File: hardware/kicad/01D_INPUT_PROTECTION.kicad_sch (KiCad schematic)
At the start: 1 part, among them U401 TPS26631PWPT CANDIDATE - NOT 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

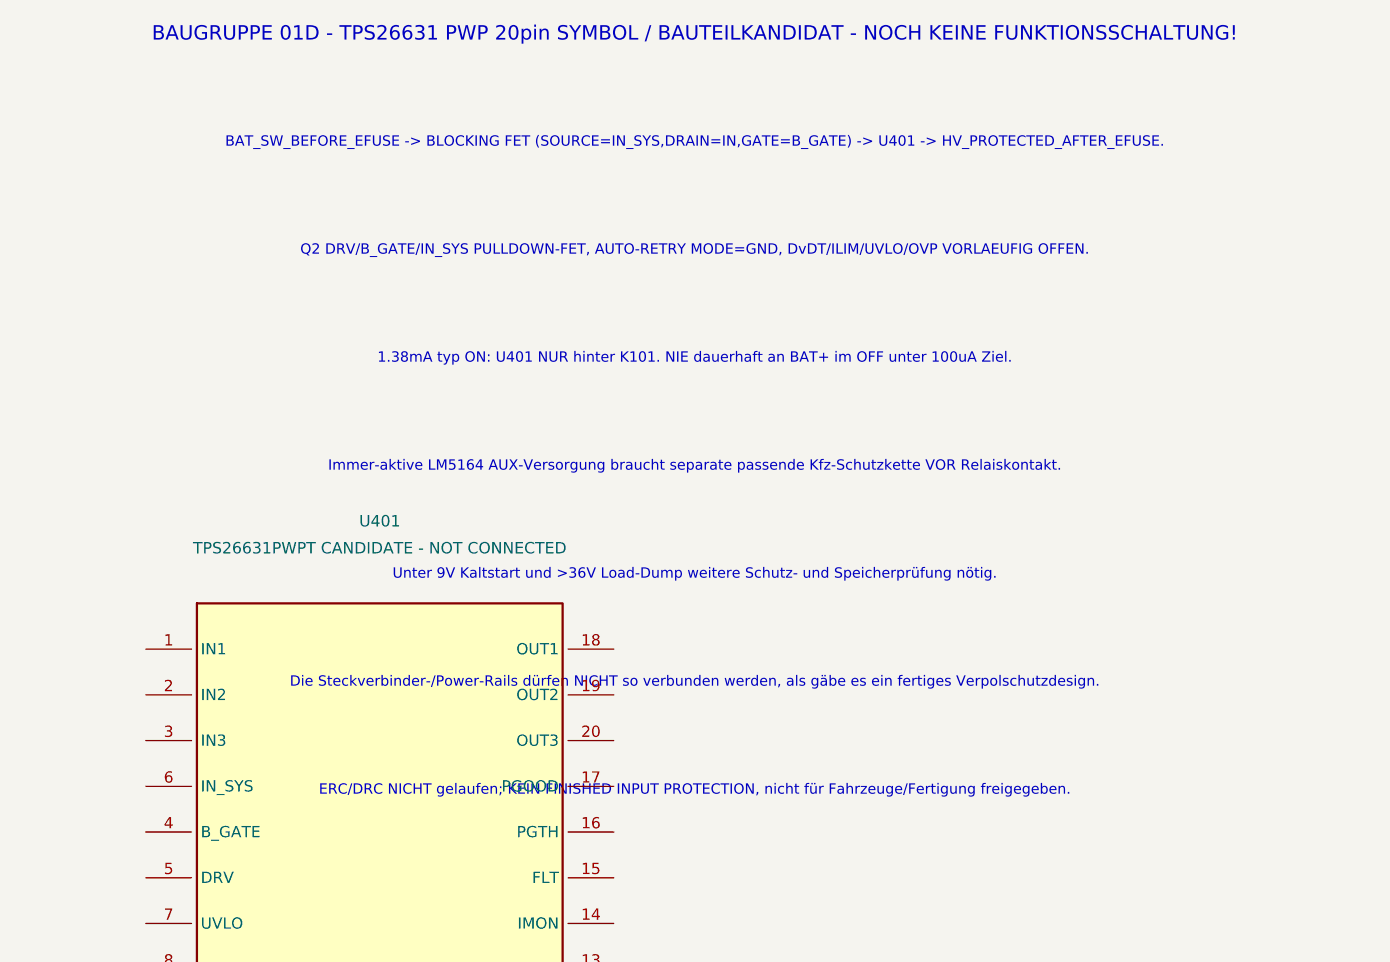
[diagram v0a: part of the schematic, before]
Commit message: kicad(power): flag relay versus eFuse overcurrent blocker in 01D
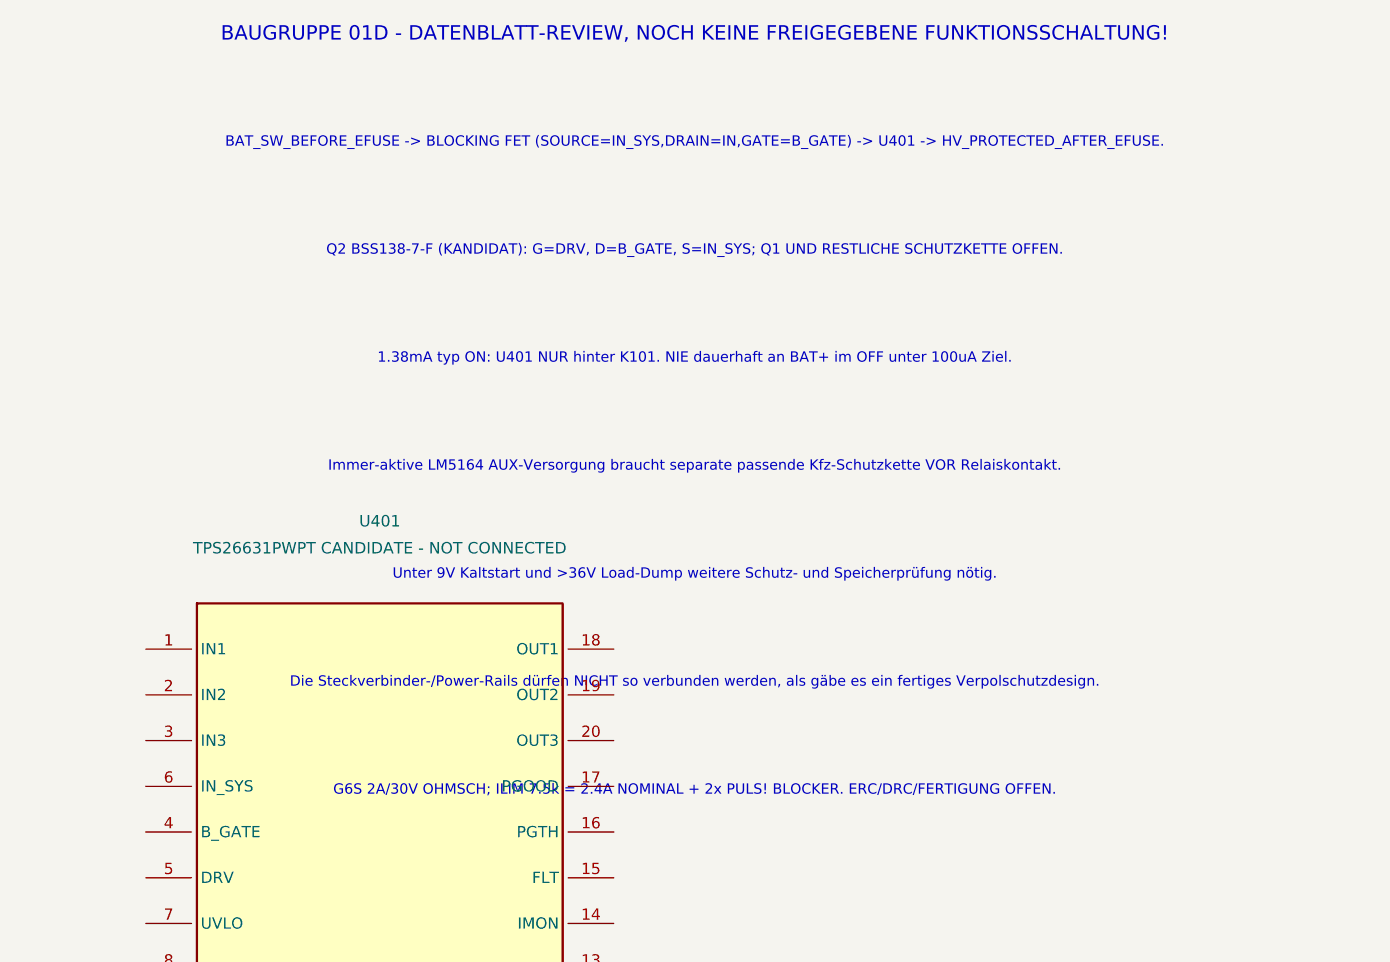
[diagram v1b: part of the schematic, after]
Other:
- note added: "BAUGRUPPE 01D - DATENBLATT-REVIEW, NOCH KEINE FREIGEGEBENE FUNKTIONSSCHALTUNG!"
- note added: "G6S 2A/30V OHMSCH; ILIM 7.5k = 2.4A NOMINAL + 2x PULS! BLOCKER. ERC/DRC/FERTIGUNG OFFEN."
- note added: "Q2 BSS138-7-F (KANDIDAT): G=DRV, D=B_GATE, S=IN_SYS; Q1 UND RESTLICHE SCHUTZKETTE OFFEN."
- note removed: "BAUGRUPPE 01D - TPS26631 PWP 20pin SYMBOL / BAUTEILKANDIDAT - NOCH KEINE FUNKTIONSSCHALTUNG!"
- note removed: "ERC/DRC NICHT gelaufen; KEIN FINISHED INPUT PROTECTION, nicht für Fahrzeuge/Fertigung freigegeben."
- note removed: "Q2 DRV/B_GATE/IN_SYS PULLDOWN-FET, AUTO-RETRY MODE=GND, DvDT/ILIM/UVLO/OVP VORLAEUFIG OFFEN."
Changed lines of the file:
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@@
 (kicad_sch (version 20250114) (generator "eeschema")
 (paper "A3")
-(title_block (title "TripTracer V1 - Eingangsschutz/eFuse Kandidat") (date "2026-10-13") (rev "a4 / SYMBOL ONLY / NOT CONNECTED / NOT ERC-TESTED"))
+(title_block (title "TripTracer V1 - Eingangsschutz/eFuse Kandidat") (date "2026-10-13") (rev "a5 / DESIGN GATE OPEN / NO WIRING / NO ERC"))
 (symbol (lib_id "TripTracer_V1:TPS26631_PWP") (at 171 112 0) (unit 1) (exclude_from_sim no) (in_bom yes) (on_board yes) (dnp no)
 (property "Reference" "U401" (at 171 80 0) (effects (font (size 1.27 1.27))))
@@
 (pin "12")
 (instances (project "TripTracer_V1" (path "/a26d9b0c-7f10-4e5a-a65f-000000000064/a26d9b0c-7f10-4e5a-a65f-000000000065/72346f29-23d6-4849-8604-2156cfdc44a1" (reference "U401") (unit 1)))))
-(text "BAUGRUPPE 01D - TPS26631 PWP 20pin SYMBOL / BAUTEILKANDIDAT - NOCH KEINE FUNKTIONSSCHALTUNG!" (at 206 26 0) (effects (font (size 1.6 1.6))))
+(text "BAUGRUPPE 01D - DATENBLATT-REVIEW, NOCH KEINE FREIGEGEBENE FUNKTIONSSCHALTUNG!" (at 206 26 0) (effects (font (size 1.6 1.6))))
 (text "BAT_SW_BEFORE_EFUSE -> BLOCKING FET (SOURCE=IN_SYS,DRAIN=IN,GATE=B_GATE) -> U401 -> HV_PROTECTED_AFTER_EFUSE." (at 206 38 0) (effects (font (size 1.15 1.15))))
-(text "Q2 DRV/B_GATE/IN_SYS PULLDOWN-FET, AUTO-RETRY MODE=GND, DvDT/ILIM/UVLO/OVP VORLAEUFIG OFFEN." (at 206 50 0) (effects (font (size 1.15 1.15))))
+(text "Q2 BSS138-7-F (KANDIDAT): G=DRV, D=B_GATE, S=IN_SYS; Q1 UND RESTLICHE SCHUTZKETTE OFFEN." (at 206 50 0) (effects (font (size 1.15 1.15))))
 (text "1.38mA typ ON: U401 NUR hinter K101. NIE dauerhaft an BAT+ im OFF unter 100uA Ziel." (at 206 62 0) (effects (font (size 1.15 1.15))))
 (text "Immer-aktive LM5164 AUX-Versorgung braucht separate passende Kfz-Schutzkette VOR Relaiskontakt." (at 206 74 0) (effects (font (size 1.15 1.15))))
 (text "Unter 9V Kaltstart und >36V Load-Dump weitere Schutz- und Speicherprüfung nötig." (at 206 86 0) (effects (font (size 1.15 1.15))))
 (text "Die Steckverbinder-/Power-Rails dürfen NICHT so verbunden werden, als gäbe es ein fertiges Verpolschutzdesign." (at 206 98 0) (effects (font (size 1.15 1.15))))
-(text "ERC/DRC NICHT gelaufen; KEIN FINISHED INPUT PROTECTION, nicht für Fahrzeuge/Fertigung freigegeben." (at 206 110 0) (effects (font (size 1.15 1.15))))
+(text "G6S 2A/30V OHMSCH; ILIM 7.5k = 2.4A NOMINAL + 2x PULS! BLOCKER. ERC/DRC/FERTIGUNG OFFEN." (at 206 110 0) (effects (font (size 1.15 1.15))))
 (sheet_instances (path "/a26d9b0c-7f10-4e5a-a65f-000000000064/a26d9b0c-7f10-4e5a-a65f-000000000065" (page "2.4")))
 (embedded_fonts no)

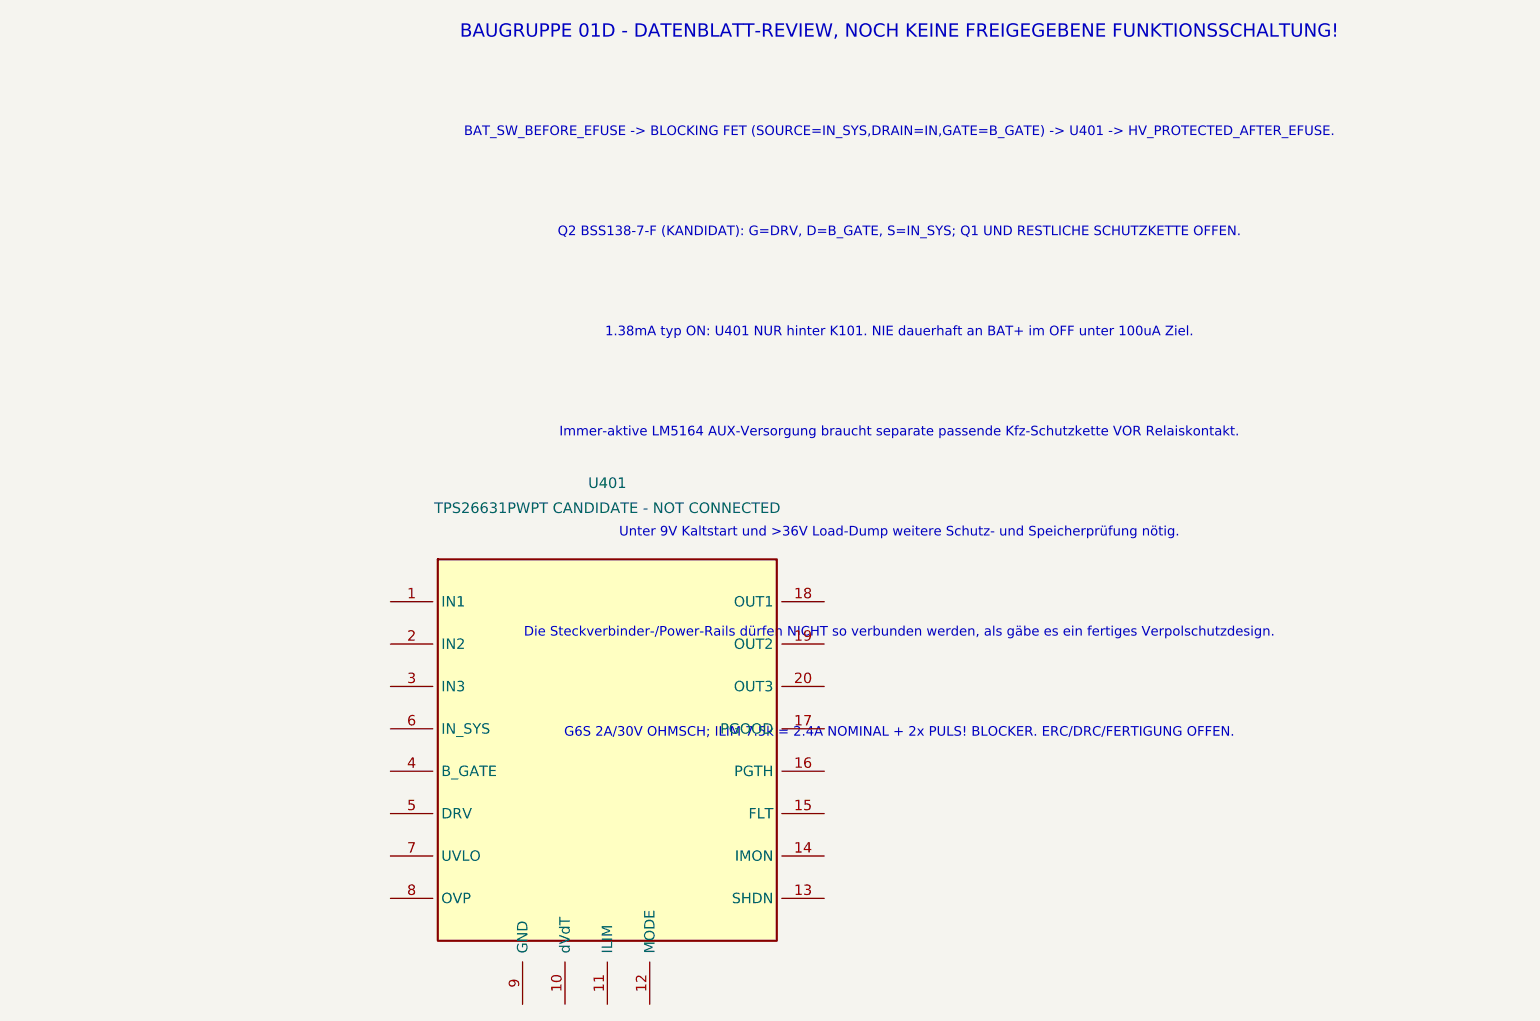
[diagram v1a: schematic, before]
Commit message: hardware(kicad): retire unconnected TPS26631 prototype from active ERC hierarchy
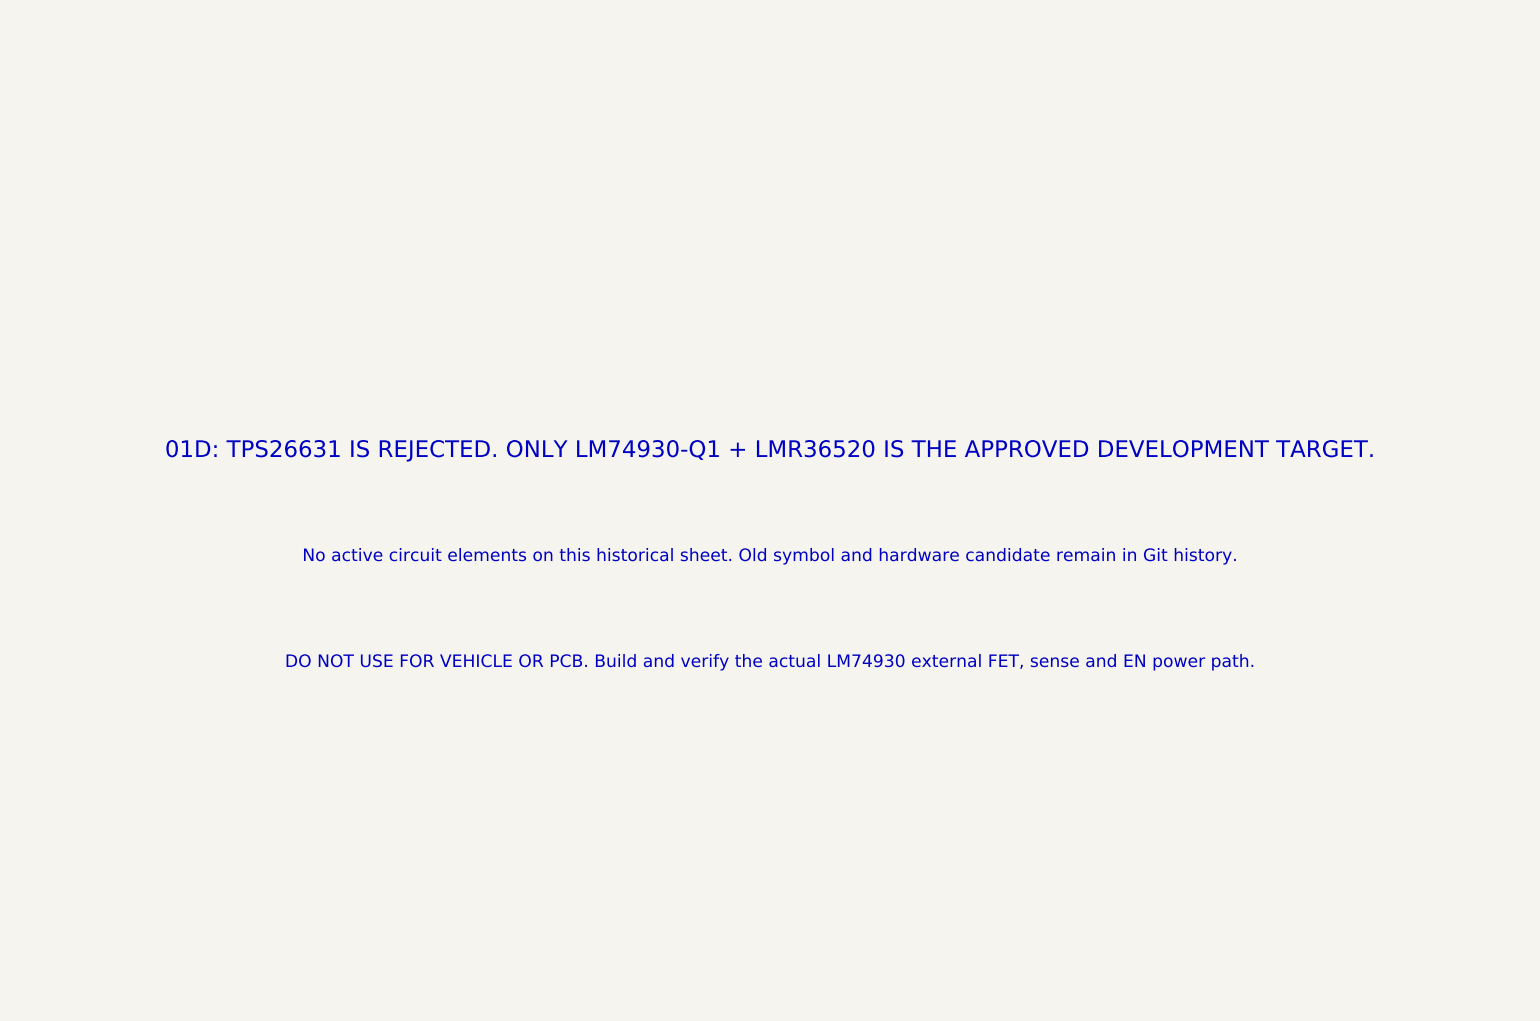
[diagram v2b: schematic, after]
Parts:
- removed U401: TPS26631PWPT CANDIDATE - NOT CONNECTED, symbol TripTracer_V1:TPS26631_PWP
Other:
- note added: "01D: TPS26631 IS REJECTED. ONLY LM74930-Q1 + LMR36520 IS THE APPROVED DEVELOPMENT TARGET."
- note added: "DO NOT USE FOR VEHICLE OR PCB. Build and verify the actual LM74930 external FET, sense and EN power path."
- note added: "No active circuit elements on this historical sheet. Old symbol and hardware candidate remain in Git history."
- note removed: "1.38mA typ ON: U401 NUR hinter K101. NIE dauerhaft an BAT+ im OFF unter 100uA Ziel."
- note removed: "BAT_SW_BEFORE_EFUSE -> BLOCKING FET (SOURCE=IN_SYS,DRAIN=IN,GATE=B_GATE) -> U401 -> HV_PROTECTED_AFTER_EFUSE."
- note removed: "BAUGRUPPE 01D - DATENBLATT-REVIEW, NOCH KEINE FREIGEGEBENE FUNKTIONSSCHALTUNG!"
- note removed: "Die Steckverbinder-/Power-Rails dürfen NICHT so verbunden werden, als gäbe es ein fertiges Verpolschutzdesign."
- note removed: "G6S 2A/30V OHMSCH; ILIM 7.5k = 2.4A NOMINAL + 2x PULS! BLOCKER. ERC/DRC/FERTIGUNG OFFEN."
- note removed: "Immer-aktive LM5164 AUX-Versorgung braucht separate passende Kfz-Schutzkette VOR Relaiskontakt."
- note removed: "Q2 BSS138-7-F (KANDIDAT): G=DRV, D=B_GATE, S=IN_SYS; Q1 UND RESTLICHE SCHUTZKETTE OFFEN."
- note removed: "Unter 9V Kaltstart und >36V Load-Dump weitere Schutz- und Speicherprüfung nötig."
- title: TripTracer V1 - Eingangsschutz/eFuse Kandidat -> TripTracer V1 - 01D retired TPS26631 candidate
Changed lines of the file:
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@@
 (kicad_sch (version 20250114) (generator "eeschema")
-(paper "A3")
-(title_block (title "TripTracer V1 - Eingangsschutz/eFuse Kandidat") (date "2026-10-13") (rev "a5 / DESIGN GATE OPEN / NO WIRING / NO ERC"))
-(symbol (lib_id "TripTracer_V1:TPS26631_PWP") (at 171 112 0) (unit 1) (exclude_from_sim no) (in_bom yes) (on_board yes) (dnp no)
-(property "Reference" "U401" (at 171 80 0) (effects (font (size 1.27 1.27))))
-(property "Value" "TPS26631PWPT CANDIDATE - NOT CONNECTED" (at 171 83 0) (effects (font (size 1.27 1.27))))
-(property "Footprint" "" (at 171 112 0) (effects (font (size 1.27 1.27)) (hide yes)))
-(pin "1")
-(pin "2")
-(pin "3")
-(pin "6")
-(pin "4")
-(pin "5")
-(pin "7")
-(pin "8")
-(pin "18")
-(pin "19")
-(pin "20")
-(pin "17")
-(pin "16")
-(pin "15")
-(pin "14")
-(pin "13")
-(pin "9")
-(pin "10")
-(pin "11")
-(pin "12")
-(instances (project "TripTracer_V1" (path "/a26d9b0c-7f10-4e5a-a65f-000000000064/a26d9b0c-7f10-4e5a-a65f-000000000065/72346f29-23d6-4849-8604-2156cfdc44a1" (reference "U401") (unit 1)))))
-(text "BAUGRUPPE 01D - DATENBLATT-REVIEW, NOCH KEINE FREIGEGEBENE FUNKTIONSSCHALTUNG!" (at 206 26 0) (effects (font (size 1.6 1.6))))
-(text "BAT_SW_BEFORE_EFUSE -> BLOCKING FET (SOURCE=IN_SYS,DRAIN=IN,GATE=B_GATE) -> U401 -> HV_PROTECTED_AFTER_EFUSE." (at 206 38 0) (effects (font (size 1.15 1.15))))
-(text "Q2 BSS138-7-F (KANDIDAT): G=DRV, D=B_GATE, S=IN_SYS; Q1 UND RESTLICHE SCHUTZKETTE OFFEN." (at 206 50 0) (effects (font (size 1.15 1.15))))
-(text "1.38mA typ ON: U401 NUR hinter K101. NIE dauerhaft an BAT+ im OFF unter 100uA Ziel." (at 206 62 0) (effects (font (size 1.15 1.15))))
-(text "Immer-aktive LM5164 AUX-Versorgung braucht separate passende Kfz-Schutzkette VOR Relaiskontakt." (at 206 74 0) (effects (font (size 1.15 1.15))))
-(text "Unter 9V Kaltstart und >36V Load-Dump weitere Schutz- und Speicherprüfung nötig." (at 206 86 0) (effects (font (size 1.15 1.15))))
-(text "Die Steckverbinder-/Power-Rails dürfen NICHT so verbunden werden, als gäbe es ein fertiges Verpolschutzdesign." (at 206 98 0) (effects (font (size 1.15 1.15))))
-(text "G6S 2A/30V OHMSCH; ILIM 7.5k = 2.4A NOMINAL + 2x PULS! BLOCKER. ERC/DRC/FERTIGUNG OFFEN." (at 206 110 0) (effects (font (size 1.15 1.15))))
-(sheet_instances (path "/a26d9b0c-7f10-4e5a-a65f-000000000064/a26d9b0c-7f10-4e5a-a65f-000000000065" (page "2.4")))
-(embedded_fonts no)
+ (paper "A3")
+ (title_block (title "TripTracer V1 - 01D retired TPS26631 candidate") (date "2026-10-14") (rev "RETired / LM74930-Q1 ONLY / NOT WIRED"))
+ (text "01D: TPS26631 IS REJECTED. ONLY LM74930-Q1 + LMR36520 IS THE APPROVED DEVELOPMENT TARGET." (at 190.5 76.2 0) (effects (font (size 2 2))))
+ (text "No active circuit elements on this historical sheet. Old symbol and hardware candidate remain in Git history." (at 190.5 88.9 0) (effects (font (size 1.5 1.5))))
+ (text "DO NOT USE FOR VEHICLE OR PCB. Build and verify the actual LM74930 external FET, sense and EN power path." (at 190.5 101.6 0) (effects (font (size 1.5 1.5))))
+ (sheet_instances (path "/a26d9b0c-7f10-4e5a-a65f-000000000064/a26d9b0c-7f10-4e5a-a65f-000000000065" (page "2.4")))
+ (embedded_fonts no)
 )
